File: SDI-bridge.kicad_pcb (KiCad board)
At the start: 6 copper layers, 70 x 33 mm, 200 parts, among them J1 031-70526-21, J2 031-70526-21, J3 WE_68715014522_ONE-SIDE, J4 MC-HVT1-S04-G, J5 MC-HVT1-S04-G, J6 MC-HVT1-S04-G, U1 MAX8902B, U2 GS2971A, U3 GS2988, U4 CrossLink_LIF-MD6000-6JMG80I, U5 SC18IS602BIPW, Y1 ABM7_27.000MH_D2Y_T

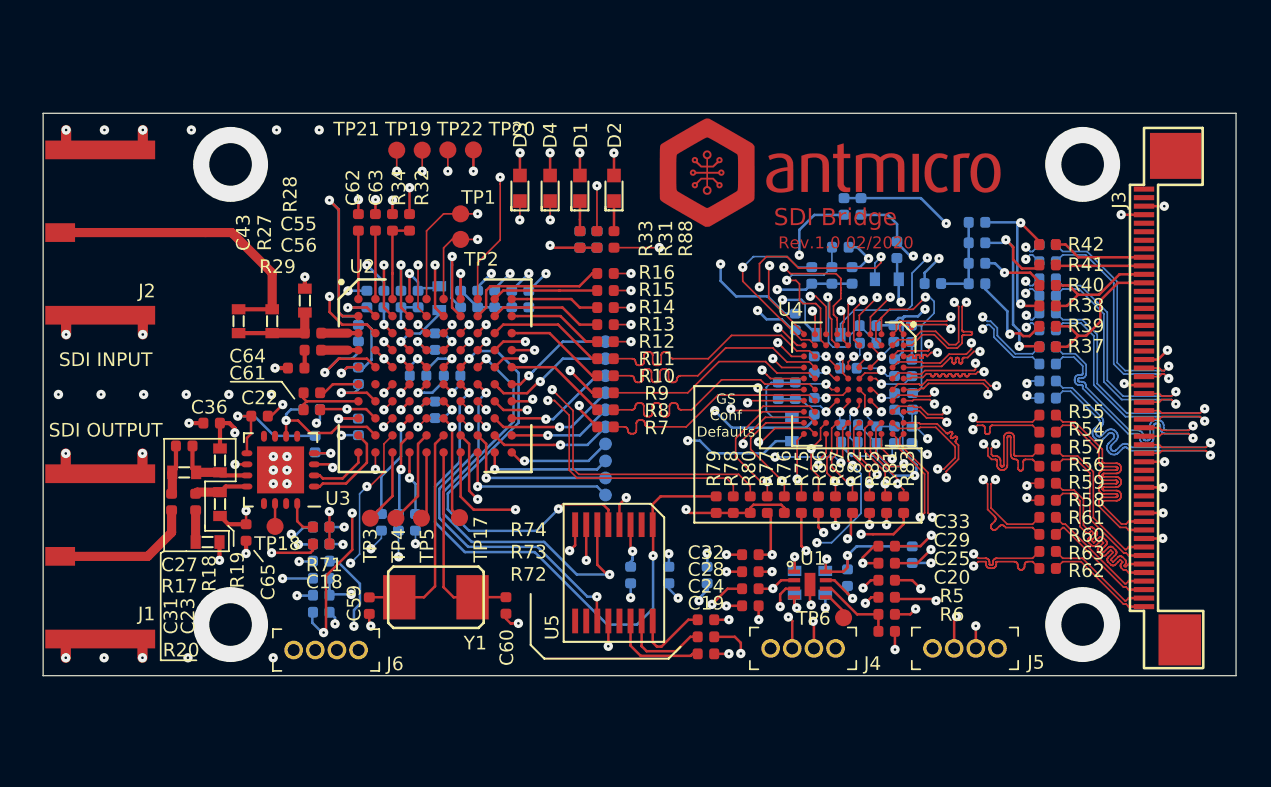
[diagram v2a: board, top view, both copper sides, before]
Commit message: Add several components to simplify the debugging process
-Add DIP switches for GS external configuration
-Make PCB a bit widther
-Move monting holes to the board sides
-Move power supply components
-Add Programming connectors
-Expose all audio pins at header
-Add GS reset button
-Add 2x user led and data error led
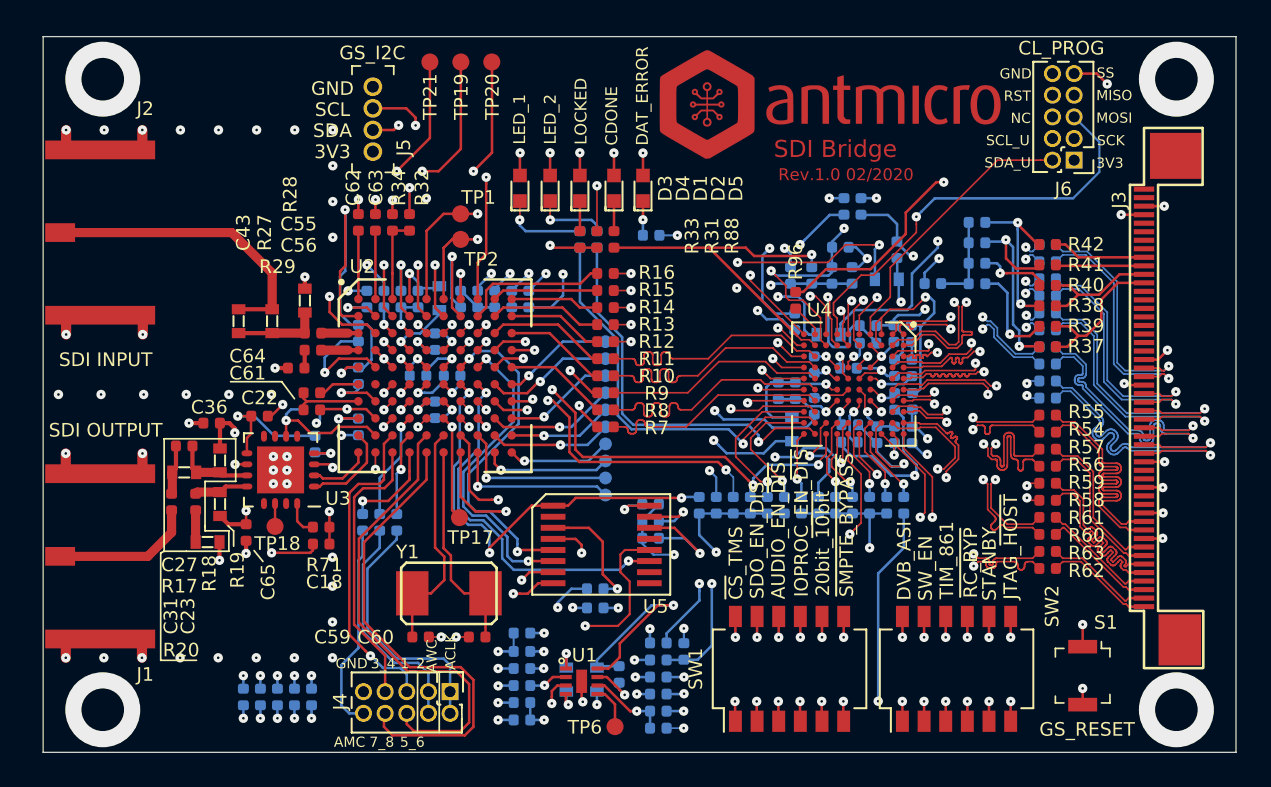
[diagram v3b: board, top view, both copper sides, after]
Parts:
- removed TP22, TP3, TP4, TP5: TP_SMD1MM, SDI-bridge-footprints:Testpoint_smd_1mm
- added D5: LG_L29K-G2J1-24-Z, SDI-bridge-footprints:LED_0603, F.Cu at (133.2, 104.4)
- added R94: R_2k2_0402, antmicro-footprints:0402-res, B.Cu at (152.8, 110.0)
- added R95: R_4k7_0402, SDI-bridge-footprints:0402-res, B.Cu at (141.9, 109.5)
- added R96: R_30R_0402, antmicro-footprints:0402-res, F.Cu at (142.2, 111.0)
- added S1: B3U-1000P, antmicro-footprints:Switch_Tactile_SMD_B3U-1000P, F.Cu at (159.0, 133.0)
- added SW1: SW_DIP_x06, antmicro-footprints:SW_SPST_6_Slide_MCDHN-06F-T-V_P1.27mm, F.Cu at (141.8, 132.6)
- added SW2: SW_DIP_x06, antmicro-footprints:SW_SPST_6_Slide_MCDHN-06F-T-V_P1.27mm, F.Cu at (151.6, 132.6)
- C19, C20, C24, C25, C28, C29, C32, C33, R5, R6, R72, R73, R74: moved to B.Cu
- J4: value MC-HVT1-S04-G -> 2199SB-10G-301523; footprint SDI-bridge-footprints:PinHeader_1x4_P1.27mm_Drill.7mm -> antmicro-footprints:PinHeader_2x05_P1.27mm_Vertical
- J6: value MC-HVT1-S04-G -> 2199SB-10G-301523; footprint antmicro-footprints:PinHeader_1x4_P1.27mm_Drill.7mm -> antmicro-footprints:PinHeader_2x05_P1.27mm_Vertical
- R64: value R_2k37_0402 -> R_100R_0402
- R65, R66, R68: value R_2k37_0402 -> R_10k_0402; footprint SDI-bridge-footprints:0402-res -> antmicro-footprints:0402-res
- R75, R76, R77, R78, R79, R80, R81, R82, R83: value R_0R_0402 -> R_10k_0402; footprint SDI-bridge-footprints:0402-res -> antmicro-footprints:0402-res; moved to B.Cu
- R84: value R_0R_0402 -> R_2k2_0402; footprint SDI-bridge-footprints:0402-res -> antmicro-footprints:0402-res
- R85, R86, R87: value R_0R_0402 -> R_2k2_0402; footprint SDI-bridge-footprints:0402-res -> antmicro-footprints:0402-res; moved to B.Cu
- moved J6 54.1 mm to (158.5, 102.8), turned to 180 degrees
- moved J5 46.8 mm to (117.3, 102.2), turned to 90 degrees
- moved R84 35.2 mm to (148.5, 123.0), turned to 90 degrees
- moved J4 22.8 mm to (121.9, 133.9), turned to 270 degrees
- moved R66 20.9 mm to (137.5, 123.0), turned to 90 degrees
- moved R64 19.1 mm to (133.7, 107.2)
- moved R65 18.5 mm to (142.5, 123.0), turned to 270 degrees
- moved R86 18.0 mm to (152.8, 107.6), turned to 0 degrees
- moved R85 17.7 mm to (152.8, 106.4), turned to 0 degrees
- moved R68 17.2 mm to (141.5, 123.0), turned to 90 degrees
- moved R87 16.4 mm to (152.8, 108.8), turned to 0 degrees
- moved R25 16.1 mm to (130.4, 129.0), turned to 0 degrees
- moved TP6 14.9 mm to (131.6, 136.0)
- moved C19 14.6 mm to (126.1, 134.6)
- moved C20 14.6 mm to (134.1, 134.1)
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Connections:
- D1 pad 2: GNDA -> GNDREF
- D2 pad 2: GNDA -> GNDREF
- D3 pad 2: GNDA -> GNDREF
- D4 pad 2: GNDA -> GNDREF
- J4 pad 1: +3V3 -> /AUDIO_SERIAL_BIT_CLK
- J4 pad 2: /SDA_CL -> /AUDIO_SERIAL_BIT_CLK
- J4 pad 3: /SCL_CL -> /AUDIO_WORD_CLK
- J4 pad 4: GNDREF -> /AUDIO_WORD_CLK
- J6 pad 1: /AUDIO_OUTPUT_CH1_2 -> +3V3
- J6 pad 2: /AUDIO_WORD_CLK -> /USER_SDA
- J6 pad 3: /AUDIO_MASTER_CLK -> /SPI_SCK(SDA)
- J6 pad 4: /AUDIO_SERIAL_BIT_CLK -> /USER_SCL
- R35 pad 1: Net-(R35-Pad1) -> /CRESET_B
- R64 pad 1: Net-(R64-Pad1) -> Net-(D5-Pad1)
- R64 pad 2: /SCL_CL -> /DATA_ERRORb
- R65 pad 1: Net-(R64-Pad1) -> /DVB_ASI
- R65 pad 2: /SDA_CL -> GNDA
- R66 pad 1: Net-(R64-Pad1) -> GNDA
- R66 pad 2: /SCL_GS -> /SDO_EN_DIS
- R67 pad 2: Net-(R64-Pad1) -> Net-(R67-Pad2)
- R68 pad 1: Net-(R64-Pad1) -> GNDA
- R68 pad 2: /SDA_GS -> /~SMPTE_BYPASS~
- R75 pad 1: /DVB_ASI -> /JTAG_~HOST~
- R76 pad 1: /~SMPTE_BYPASS~ -> GNDA
- R76 pad 2: IO_VDD -> /20bit_~10bit~
- R77 pad 1: /20bit_~10bit~ -> /STANDBY
- R78 pad 1: /Audio_EN_~DIS~ -> GNDA
- R78 pad 2: IO_VDD -> /IOPROC_EN_~DIS~
- R79 pad 1: /~CS~_TMS -> /~RC_BYP~
- R79 pad 2: IO_VDD -> GNDA
- R80 pad 1: /IOPROC_EN_~DIS~ -> GNDA
- R80 pad 2: IO_VDD -> /Audio_EN_~DIS~
- R81 pad 1: /JTAG_~HOST~ -> /TIM_861
- R82 pad 1: /~RC_BYP~ -> GNDA
- R82 pad 2: IO_VDD -> /~CS~_TMS
- R83 pad 1: /RST_TRST -> /SW_EN
- R83 pad 2: IO_VDD -> GNDA
- R84 pad 1: /SDO_EN_DIS -> IO_VDD
- R84 pad 2: IO_VDD -> /RST_TRST
- R85 pad 1: /STANDBY -> Net-(R67-Pad2)
- R85 pad 2: GNDA -> /SCL_CL
- R86 pad 1: /SW_EN -> Net-(R67-Pad2)
- R86 pad 2: IO_VDD -> /SDA_CL
- R87 pad 1: /TIM_861 -> Net-(R67-Pad2)
- R87 pad 2: IO_VDD -> /SCL_GS
- R89 pad 2: Net-(R35-Pad1) -> /CRESET_B
- U4 pad D1: /IOPROC_EN_~DIS~ -> /USER_SDA
- U4 pad G1: /LED_1 -> /MOSI
- U4 pad H1: /SCL_CL -> /SPI_SS(SCL)
- U4 pad H10: /AUDIO_SERIAL_BIT_CLK -> /IOPROC_EN_~DIS~
- U4 pad H2: Net-(R35-Pad1) -> /CRESET_B
- U4 pad J1: /SDA_CL -> Net-(R96-Pad2)
- U4 pad J10: /AUDIO_OUTPUT_CH1_2 -> /LED_2
- U4 pad J8: /AUDIO_WORD_CLK -> /Audio_EN_~DIS~
- U4 pad J9: /AUDIO_MASTER_CLK -> /LED_1
- U4 pad K1: /LED_2 -> /MISO
- U4 pad K2: /Audio_EN_~DIS~ -> /USER_SCL
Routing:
- net /SCL_CL: track 65.5 -> 9.77 mm, vias 4 -> 2
- net /SDA_CL: track 62.3 -> 12.4 mm, vias 4 -> 2
- net /SDA_GS: track 52.7 -> 97.2 mm
- net /SDO_EN_DIS: track 8.31 -> 49.9 mm, vias 1 -> 3
- net /SCL_GS: track 55.5 -> 96.7 mm
- net /MISO: track 0.00 -> 35.8 mm, vias 0 -> 1
- net /SPI_SS(SCL): track 0.00 -> 35.2 mm, vias 0 -> 3
- net /CRESET_B: track 0.00 -> 29.0 mm, vias 0 -> 2
- net /AUDIO_OUTPUT_CH1_2: track 46.6 -> 18.8 mm, vias 3 -> 1
- net /AUDIO_WORD_CLK: track 38.9 -> 13.5 mm, vias 2 -> 0
- net /MOSI: track 0.00 -> 25.1 mm, vias 0 -> 1
- net /SPI_SCK(SDA): track 0.00 -> 24.6 mm, vias 0 -> 1
- net /AUDIO_OUTPUT_CH7_8: track 3.98 -> 28.5 mm
- net /AUDIO_MASTER_CLK: track 36.7 -> 12.3 mm, vias 2 -> 0
- net /USER_SCL: track 0.00 -> 23.1 mm, vias 0 -> 1
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- added copper zone on In3.Cu, net GNDA
- removed copper zone on In1.Cu, net GNDA
- removed copper zone on In3.Cu, net GNDREF
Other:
- board size 70 x 33 mm -> 70 x 42 mm
- board text added: "1_2"
- board text added: "20bit_~10bit~"
- board text added: "3V3"
- board text added: "3_4"
- board text added: "5_6"
- board text added: "7_8"
- board text added: "ACLK"
- board text added: "AMC"
- board text added: "AUDIO_EN_~DIS~"
- board text added: "AWC"
- board text added: "CDONE"
- board text added: "CL_PROG"
- board text added: "DAT_ERROR"
- board text added: "DVB_ASI"
- board text added: "GND"
- board text added: "GS_I2C"
- board text added: "GS_RESET"
- board text added: "IOPROC_EN_~DIS~"
- board text added: "JTAG_~HOST~"
- board text added: "LED_1"
- board text added: "LED_2"
- board text added: "LOCKED"
- board text added: "MISO"
- board text added: "MOSI"
- board text added: "NC"
- board text added: "RST"
- board text added: "SCK"
- board text added: "SCL"
- board text added: "SCL_U"
- board text added: "SDA"
- board text added: "SDA_U"
- board text added: "SDO_EN_DIS"
- board text added: "SS"
- board text added: "STANBY"
- board text added: "SW_EN"
- board text added: "TIM_861"
- board text added: "~CS~_TMS"
- board text added: "~RC_BYP~"
- board text added: "~SMPTE_BYPASS~"
- board text removed: "GS Conf Defaults"

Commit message: Update revision info on PCB
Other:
- board text added: "Rev.1.0.0 04/2020"
- board text removed: "Rev.1.0 02/2020"
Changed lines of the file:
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@@
-(kicad_pcb (version 20171130) (host pcbnew 5.1.5+dfsg1-2~bpo10+1)
+(kicad_pcb (version 20171130) (host pcbnew 5.1.4+dfsg1-1~bpo10+1)
   (general
     (thickness 1.6)
     (drawings 87)
-    (tracks 4684)
+    (tracks 4686)
     (zones 0)
     (modules 203)
@@
   (page A4)
   (layers
-    (0 F.Cu signal hide)
-    (1 In1.Cu power hide)
-    (2 In2.Cu power)
-    (3 In3.Cu signal hide)
-    (4 In4.Cu signal hide)
-    (31 B.Cu signal hide)
+    (0 F.Cu signal)
+    (1 In1.Cu power)
+    (2 In2.Cu power hide)
+    (3 In3.Cu signal)
+    (4 In4.Cu signal)
+    (31 B.Cu signal)
     (32 B.Adhes user hide)
     (33 F.Adhes user hide)
@@
     (37 F.SilkS user hide)
     (38 B.Mask user hide)
-    (39 F.Mask user hide)
+    (39 F.Mask user)
     (40 Dwgs.User user hide)
     (41 Cmts.User user hide)
@@
   )
   (setup
-    (last_trace_width 0.15)
+    (last_trace_width 0.1)
     (user_trace_width 0.1)
     (user_trace_width 0.125)
@@
   (gr_line (start 154.14 124.39) (end 152 122.25) (layer B.SilkS) (width 0.1))
   (gr_line (start 156.08 124.39) (end 154.14 124.39) (layer B.SilkS) (width 0.1))
-  (gr_text "Rev.1.0 02/2020" (at 145.11 103.6) (layer F.Mask)
+  (gr_text "Rev.1.0.0 04/2020" (at 145.5234 103.6068) (layer F.Mask)
     (effects (font (size 0.7 0.7) (thickness 0.15)))
   )
@@
     (effects (font (size 1 1) (thickness 0.2)))
   )
-  (gr_text "Rev.1.0 02/2020" (at 145.11 103.6) (layer F.Cu)
+  (gr_text "Rev.1.0.0 04/2020" (at 145.5234 103.6068) (layer F.Cu)
     (effects (font (size 0.7 0.7) (thickness 0.15)))
   )
@@
   (segment (start 145.69758 107.86) (end 146.35999 108.52241) (width 0.15) (layer B.Cu) (net 1))
   (segment (start 145.47 109.03) (end 145.8524 109.03) (width 0.15) (layer B.Cu) (net 1))
+  (via (at 129.495 102.315) (size 0.55) (drill 0.15) (layers F.Cu B.Cu) (net 1))
+  (segment (start 129.5 103.65) (end 129.5 102.32) (width 0.15) (layer F.Cu) (net 1))
+  (segment (start 129.5 102.32) (end 129.495 102.315) (width 0.15) (layer F.Cu) (net 1))
+  (via (at 131.495 102.325) (size 0.55) (drill 0.15) (layers F.Cu B.Cu) (net 1))
+  (segment (start 131.5 103.65) (end 131.5 102.33) (width 0.15) (layer F.Cu) (net 1))
+  (segment (start 131.5 102.33) (end 131.495 102.325) (width 0.15) (layer F.Cu) (net 1))
+  (via (at 127.75 102.32) (size 0.55) (drill 0.15) (layers F.Cu B.Cu) (net 1))
+  (segment (start 127.75 103.65) (end 127.75 102.32) (width 0.15) (layer F.Cu) (net 1))
+  (via (at 125.99 102.32) (size 0.55) (drill 0.15) (layers F.Cu B.Cu) (net 1))
+  (segment (start 125.98 103.65) (end 125.98 102.33) (width 0.15) (layer F.Cu) (net 1))
+  (segment (start 125.98 102.33) (end 125.99 102.32) (width 0.15) (layer F.Cu) (net 1))
+  (via (at 133.2 102.33) (size 0.55) (drill 0.15) (layers F.Cu B.Cu) (net 1))
+  (segment (start 133.2 103.65) (end 133.2 102.33) (width 0.15) (layer F.Cu) (net 1))
   (via (at 146.3825 114.265) (size 0.55) (drill 0.15) (layers F.Cu B.Cu) (net 2))
   (via (at 146.3825 117.515) (size 0.55) (drill 0.15) (layers F.Cu B.Cu) (net 2))
@@
   (segment (start 116.5 105.915) (end 116.5 105.07) (width 0.15) (layer F.Cu) (net 3))
   (segment (start 116.5 105.07) (end 116.505 105.065) (width 0.15) (layer F.Cu) (net 3))
-  (via (at 129.495 102.315) (size 0.55) (drill 0.15) (layers F.Cu B.Cu) (net 1))
-  (segment (start 129.5 103.65) (end 129.5 102.32) (width 0.15) (layer F.Cu) (net 1))
-  (segment (start 129.5 102.32) (end 129.495 102.315) (width 0.15) (layer F.Cu) (net 1))
-  (via (at 131.495 102.325) (size 0.55) (drill 0.15) (layers F.Cu B.Cu) (net 1))
-  (segment (start 131.5 103.65) (end 131.5 102.33) (width 0.15) (layer F.Cu) (net 1))
-  (segment (start 131.5 102.33) (end 131.495 102.325) (width 0.15) (layer F.Cu) (net 1))
   (via (at 127.385 131.585) (size 0.55) (drill 0.15) (layers F.Cu B.Cu) (net 3))
   (segment (start 126.585 131.58) (end 127.38 131.58) (width 0.15) (layer B.Cu) (net 3))
@@
   (via (at 115.89 110.42) (size 0.55) (drill 0.15) (layers F.Cu B.Cu) (net 3))
   (segment (start 115.89 110.42) (end 115.895 110.415) (width 0.15) (layer B.Cu) (net 3))
-  (via (at 127.75 102.32) (size 0.55) (drill 0.15) (layers F.Cu B.Cu) (net 1))
-  (segment (start 127.75 103.65) (end 127.75 102.32) (width 0.15) (layer F.Cu) (net 1))
-  (via (at 125.99 102.32) (size 0.55) (drill 0.15) (layers F.Cu B.Cu) (net 1))
-  (segment (start 125.98 103.65) (end 125.98 102.33) (width 0.15) (layer F.Cu) (net 1))
-  (segment (start 125.98 102.33) (end 125.99 102.32) (width 0.15) (layer F.Cu) (net 1))
   (segment (start 117.5 113.9) (end 118 114.4) (width 0.15) (layer F.Cu) (net 3))
   (via (at 114.53 115.21) (size 0.55) (drill 0.15) (layers F.Cu B.Cu) (net 3))
@@
   (via (at 137.5 125.75) (size 0.55) (drill 0.15) (layers F.Cu B.Cu) (net 3))
   (segment (start 136.5 124.75) (end 137.5 125.75) (width 0.15) (layer B.Cu) (net 3))
-  (via (at 133.2 102.33) (size 0.55) (drill 0.15) (layers F.Cu B.Cu) (net 1))
-  (segment (start 133.2 103.65) (end 133.2 102.33) (width 0.15) (layer F.Cu) (net 1))
   (segment (start 133.61 131.075) (end 133.61 130.35) (width 0.15) (layer B.Cu) (net 3))
   (segment (start 133.615 131.08) (end 133.61 131.075) (width 0.15) (layer B.Cu) (net 3))
@@
   (segment (start 158.5 101.48) (end 159.43 101.48) (width 0.15) (layer In2.Cu) (net 204))
   (segment (start 159.43 101.48) (end 159.99 102.04) (width 0.15) (layer In2.Cu) (net 204))
-  (segment (start 150.408059 104.04) (end 150.85 104.04) (width 0.15) (layer F.Cu) (net 204))
   (segment (start 142.598998 110.485) (end 143.933998 109.15) (width 0.15) (layer F.Cu) (net 204))
   (segment (start 148.62 107.08) (end 148.62 105.828059) (width 0.15) (layer F.Cu) (net 204))
@@
   (segment (start 146.55 109.15) (end 148.62 107.08) (width 0.15) (layer F.Cu) (net 204))
   (segment (start 142.16 110.485) (end 142.598998 110.485) (width 0.15) (layer F.Cu) (net 204))
-  (segment (start 148.62 105.828059) (end 150.408059 104.04) (width 0.15) (layer F.Cu) (net 204))
+  (segment (start 148.62 105.828059) (end 149.160229 105.287829) (width 0.15) (layer F.Cu) (net 204))
+  (segment (start 149.160229 105.287829) (end 150.281271 105.287829) (width 0.15) (layer F.Cu) (net 204))
+  (segment (start 150.85 104.7191) (end 150.85 104.04) (width 0.15) (layer F.Cu) (net 204))
+  (segment (start 150.281271 105.287829) (end 150.85 104.7191) (width 0.15) (layer F.Cu) (net 204))
   (segment (start 156.522894 102.75) (end 157.23 102.75) (width 0.1) (layer F.Cu) (net 205))
   (segment (start 154.005 102.75) (end 156.522894 102.75) (width 0.1) (layer F.Cu) (net 205))
